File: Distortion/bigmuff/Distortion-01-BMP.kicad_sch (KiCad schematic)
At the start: 46 parts, among them J1 Conn_01x04_Female, Q1 2N5088, Q2 2N5088, Q4 2N5088, Q5 2N5088

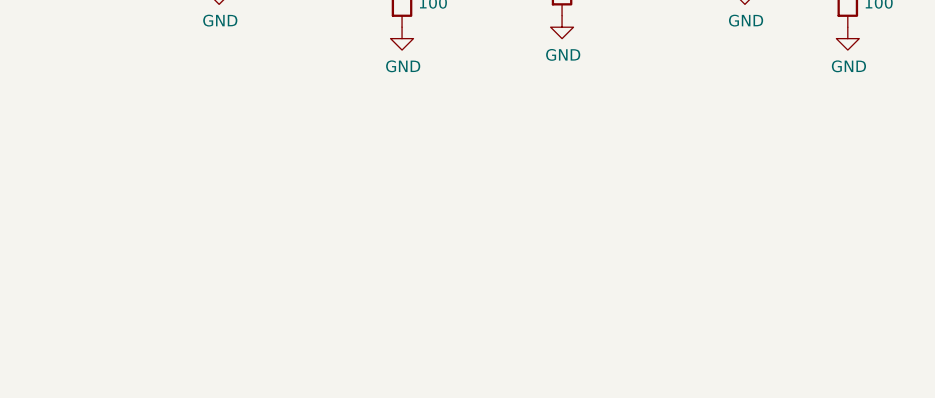
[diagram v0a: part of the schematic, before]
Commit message: fix to badmonkey -- pedal works but the schematic this was based on does not seem right.   There's a voltage offset on the input when engaged, and this messes with it in the pedal chain.
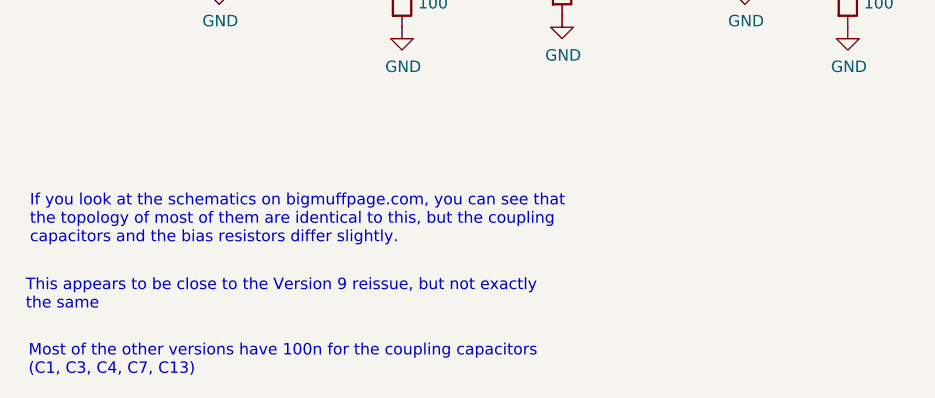
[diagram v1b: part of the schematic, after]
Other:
- note added: "If you look at the schematics on bigmuffpage.com, you can see that the topology of most of them are identical to this, but the coupling capacitors and the bias resistors differ slightly."
- note added: "Most of the other versions have 100n for the coupling capacitors (C1, C3, C4, C7, C13)"
- note added: "This appears to be close to the Version 9 reissue, but not exactly the same"
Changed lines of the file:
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@@
     (stroke (width 0) (type default))
+  )
+  (text "Most of the other versions have 100n for the coupling capacitors\n(C1, C3, C4, C7, C13)\n"
+    (at 23.2664 153.1112 0)
+    (effects (font (size 1.27 1.27)) (justify left bottom))
+  )
+  (text "\nIf you look at the schematics on bigmuffpage.com, you can see that \nthe topology of most of them are identical to this, but the coupling \ncapacitors and the bias resistors differ slightly.   \n"
+    (at 23.4188 138.4808 0)
+    (effects (font (size 1.27 1.27)) (justify left bottom))
+  )
+  (text "This appears to be close to the Version 9 reissue, but not exactly \nthe same\n"
+    (at 22.9616 145.8468 0)
+    (effects (font (size 1.27 1.27)) (justify left bottom))
   )
   (global_label "IN" (shape input) (at 224.79 41.91 180)
